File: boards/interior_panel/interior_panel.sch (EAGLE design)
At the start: 28 parts, among them IC1 LM2576, IC2 DS1307, J1 POWER_JACKPTH_BREAD, Q1 MOSFET-NCHANNELFQP30N06L, U1 ATMEGA328P, U2 EXT ENCLOSURE, U3 DISPLAY, Y1 16MHz, Y2 32.786kHz

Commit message: PCB Update
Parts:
- C5: device nerdvellous-capacitors:CAP-1000UF -> nerdvellous-capacitors:CAP-1000UF16V
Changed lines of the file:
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@@
 <grid distance="0.1" unitdist="inch" unit="inch" style="lines" multiple="1" display="no" altdistance="0.01" altunitdist="inch" altunit="inch"/>
 <layers>
-<layer number="1" name="Top" color="4" fill="1" visible="no" active="no"/>
-<layer number="16" name="Bottom" color="1" fill="1" visible="no" active="no"/>
-<layer number="17" name="Pads" color="2" fill="1" visible="no" active="no"/>
-<layer number="18" name="Vias" color="2" fill="1" visible="no" active="no"/>
-<layer number="19" name="Unrouted" color="6" fill="1" visible="no" active="no"/>
-<layer number="20" name="Dimension" color="15" fill="1" visible="no" active="no"/>
-<layer number="21" name="tPlace" color="7" fill="1" visible="no" active="no"/>
-<layer number="22" name="bPlace" color="7" fill="1" visible="no" active="no"/>
-<layer number="23" name="tOrigins" color="15" fill="1" visible="no" active="no"/>
-<layer number="24" name="bOrigins" color="15" fill="1" visible="no" active="no"/>
-<layer number="25" name="tNames" color="7" fill="1" visible="no" active="no"/>
-<layer number="26" name="bNames" color="7" fill="1" visible="no" active="no"/>
-<layer number="27" name="tValues" color="7" fill="1" visible="no" active="no"/>
-<layer number="28" name="bValues" color="7" fill="1" visible="no" active="no"/>
+<layer number="1" name="Top" color="4" fill="1" visible="yes" active="no"/>
+<layer number="16" name="Bottom" color="1" fill="1" visible="yes" active="no"/>
+<layer number="17" name="Pads" color="2" fill="1" visible="yes" active="no"/>
+<layer number="18" name="Vias" color="2" fill="1" visible="yes" active="no"/>
+<layer number="19" name="Unrouted" color="6" fill="1" visible="yes" active="no"/>
+<layer number="20" name="Dimension" color="15" fill="1" visible="yes" active="no"/>
+<layer number="21" name="tPlace" color="16" fill="1" visible="yes" active="no"/>
+<layer number="22" name="bPlace" color="14" fill="1" visible="yes" active="no"/>
+<layer number="23" name="tOrigins" color="15" fill="1" visible="yes" active="no"/>
+<layer number="24" name="bOrigins" color="15" fill="1" visible="yes" active="no"/>
+<layer number="25" name="tNames" color="7" fill="1" visible="yes" active="no"/>
+<layer number="26" name="bNames" color="7" fill="1" visible="yes" active="no"/>
+<layer number="27" name="tValues" color="7" fill="1" visible="yes" active="no"/>
+<layer number="28" name="bValues" color="7" fill="1" visible="yes" active="no"/>
 <layer number="29" name="tStop" color="7" fill="3" visible="no" active="no"/>
 <layer number="30" name="bStop" color="7" fill="6" visible="no" active="no"/>
@@
 <layer number="35" name="tGlue" color="7" fill="4" visible="no" active="no"/>
 <layer number="36" name="bGlue" color="7" fill="5" visible="no" active="no"/>
-<layer number="37" name="tTest" color="7" fill="1" visible="no" active="no"/>
-<layer number="38" name="bTest" color="7" fill="1" visible="no" active="no"/>
+<layer number="37" name="tTest" color="7" fill="1" visible="yes" active="no"/>
+<layer number="38" name="bTest" color="7" fill="1" visible="yes" active="no"/>
 <layer number="39" name="tKeepout" color="4" fill="11" visible="no" active="no"/>
 <layer number="40" name="bKeepout" color="1" fill="11" visible="no" active="no"/>
@@
 <layer number="44" name="Drills" color="7" fill="1" visible="no" active="no"/>
 <layer number="45" name="Holes" color="7" fill="1" visible="no" active="no"/>
-<layer number="46" name="Milling" color="3" fill="1" visible="no" active="no"/>
-<layer number="47" name="Measures" color="7" fill="1" visible="no" active="no"/>
-<layer number="48" name="Document" color="7" fill="1" visible="no" active="no"/>
-<layer number="49" name="Reference" color="7" fill="1" visible="no" active="no"/>
-<layer number="50" name="dxf" color="7" fill="1" visible="no" active="no"/>
-<layer number="51" name="tDocu" color="7" fill="1" visible="no" active="no"/>
-<layer number="52" name="bDocu" color="7" fill="1" visible="no" active="no"/>
-<layer number="53" name="tGND_GNDA" color="7" fill="9" visible="no" active="no"/>
-<layer number="54" name="bGND_GNDA" color="1" fill="9" visible="no" active="no"/>
-<layer number="56" name="wert" color="7" fill="1" visible="no" active="no"/>
-<layer number="57" name="tCAD" color="7" fill="1" visible="no" active="no"/>
+<layer number="46" name="Milling" color="3" fill="1" visible="yes" active="no"/>
+<layer number="47" name="Measures" color="7" fill="1" visible="yes" active="no"/>
+<layer number="48" name="Document" color="7" fill="1" visible="yes" active="no"/>
+<layer number="49" name="Reference" color="7" fill="1" visible="yes" active="no"/>
+<layer number="50" name="dxf" color="7" fill="1" visible="yes" active="no"/>
+<layer number="51" name="tDocu" color="6" fill="1" visible="yes" active="no"/>
+<layer number="52" name="bDocu" color="7" fill="1" visible="yes" active="no"/>
+<layer number="53" name="tGND_GNDA" color="7" fill="9" visible="yes" active="no"/>
+<layer number="54" name="bGND_GNDA" color="1" fill="9" visible="yes" active="no"/>
+<layer number="56" name="wert" color="7" fill="1" visible="yes" active="no"/>
+<layer number="57" name="tCAD" color="7" fill="1" visible="yes" active="no"/>
 <layer number="90" name="Modules" color="5" fill="1" visible="yes" active="yes"/>
 <layer number="91" name="Nets" color="2" fill="1" visible="yes" active="yes"/>
@@
 <part name="Y2" library="nerdvellous-electromechanical" deviceset="CRYSTAL" device="TC26V" value="32.786kHz"/>
 <part name="GND15" library="nerdvellous-schematics" deviceset="GND" device=""/>
-<part name="C5" library="nerdvellous-capacitors" deviceset="CAP-1000UF" device="" value="1000uF"/>
+<part name="C5" library="nerdvellous-capacitors" deviceset="CAP-1000UF" device="16V" value="1000uF"/>
 <part name="BAT1" library="nerdvellous-electromechanical" deviceset="BATTERY" device="12MMFULLPTH"/>
 <part name="LED1" library="nerdvellous-led" deviceset="LED" device="5MM" value="RED"/>

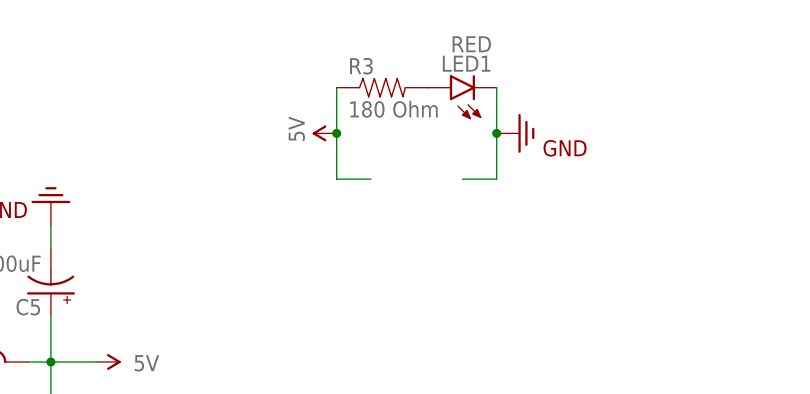
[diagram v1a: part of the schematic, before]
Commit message: 100 Ohm resistor for the power led
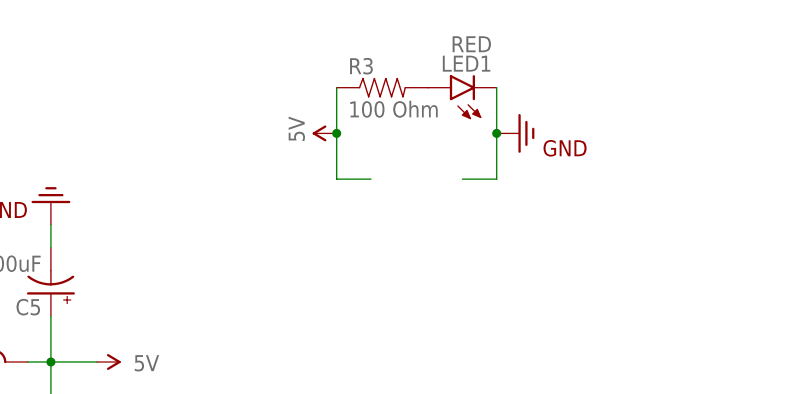
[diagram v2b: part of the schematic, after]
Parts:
- JP1: value M02JST-PTH-VERT -> M02PTH; device nerdvellous-connectors:M02JST-PTH-VERT -> nerdvellous-connectors:M02PTH
- R3: value 180 Ohm -> 100 Ohm; device nerdvellous-resistors:RES-180OHM -> nerdvellous-resistors:RES-100OHM
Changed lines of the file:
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@@
 <class number="0" name="default" width="0" drill="0">
+</class>
+<class number="1" name="power5V" width="0.8128" drill="0">
 </class>
 </classes>
@@
 <part name="SUPPLY3" library="nerdvellous_schematics" deviceset="12V" device=""/>
 <part name="Q1" library="nerdvellous-transistors" deviceset="MOSFET-NCHANNEL" device="FQP30N06L"/>
-<part name="JP1" library="nerdvellous-connectors" deviceset="M02" device="JST-PTH-VERT"/>
+<part name="JP1" library="nerdvellous-connectors" deviceset="M02" device="PTH" value="M02PTH"/>
 <part name="SUPPLY4" library="nerdvellous-schematics" deviceset="12V" device=""/>
 <part name="GND7" library="nerdvellous-schematics" deviceset="GND" device=""/>
@@
 <part name="LED1" library="nerdvellous-led" deviceset="LED" device="5MM" value="RED"/>
 <part name="GND16" library="nerdvellous-schematics" deviceset="GND" device=""/>
-<part name="R3" library="nerdvellous-resistors" deviceset="RES-180OHM" device="" value="180 Ohm"/>
+<part name="R3" library="nerdvellous-resistors" deviceset="RES-100OHM" device="" value="100 Ohm"/>
 <part name="SUPPLY12" library="nerdvellous-schematics" deviceset="5V" device=""/>
 <part name="C2" library="nerdvellous-capacitors" deviceset="CAP-0.1UF" device="" value="0.1uF"/>
@@
 </segment>
 </net>
-<net name="5V" class="0">
+<net name="5V" class="1">
 <segment>
 <pinref part="L1" gate="G$1" pin="2"/>
